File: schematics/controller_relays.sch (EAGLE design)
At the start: 6 parts, among them K1 D1225, K2 D1225, K3 D1225

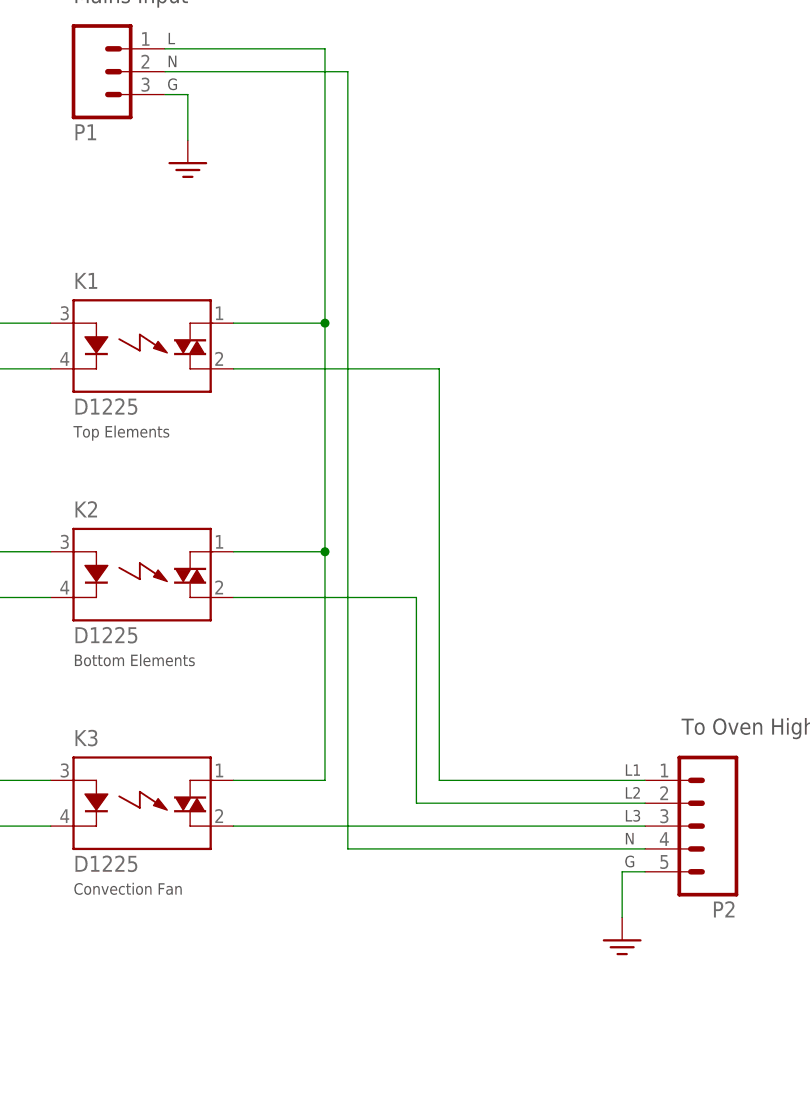
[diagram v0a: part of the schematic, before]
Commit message: Update earth and chassis ground symbols.
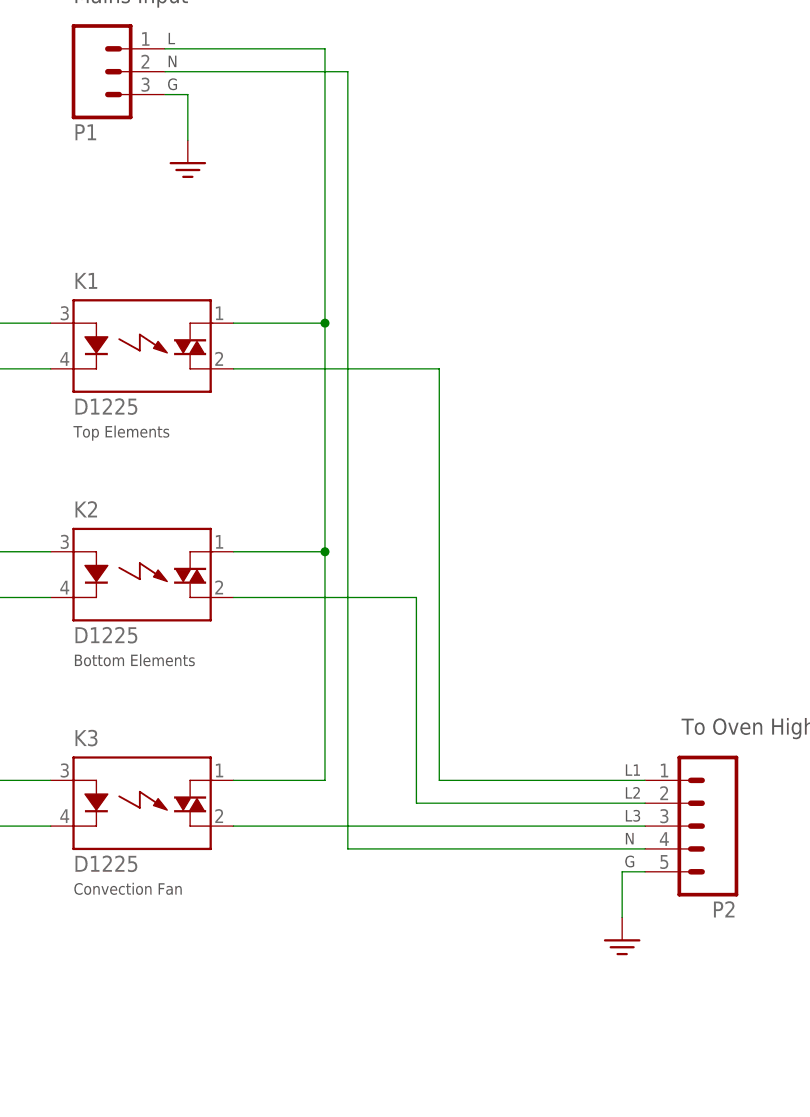
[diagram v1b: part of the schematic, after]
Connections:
- net 3.3V renamed GND
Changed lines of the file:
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@@
 <part name="P1" library="con-amp-quick" library_urn="urn:adsk.eagle:library:125" deviceset="MA03" device="" package3d_urn="urn:adsk.eagle:package:5957/1"/>
 <part name="P2" library="con-amp-quick" library_urn="urn:adsk.eagle:library:125" deviceset="MA05" device="" package3d_urn="urn:adsk.eagle:package:5972/1"/>
-<part name="GND1" library="SparkFun-PowerSymbols" deviceset="GND2" device="" value=""/>
-<part name="GND2" library="SparkFun-PowerSymbols" deviceset="GND2" device="" value=""/>
+<part name="GND1" library="supply" deviceset="EGND" device=""/>
+<part name="GND2" library="supply" deviceset="EGND" device=""/>
 </parts>
 <sheets>
@@
 <instance part="P1" gate="G$1" x="121.92" y="152.4" rot="MR180"/>
 <instance part="P2" gate="G$1" x="190.5" y="68.58" rot="R180"/>
-<instance part="GND1" gate="G$1" x="132.08" y="142.24"/>
-<instance part="GND2" gate="G$1" x="180.34" y="55.88"/>
+<instance part="GND1" gate="1" x="132.08" y="142.24"/>
+<instance part="GND2" gate="1" x="180.34" y="55.88"/>
 </instances>
 <busses>
@@
 <pinref part="K1" gate="G$1" pin="K"/>
 <wire x1="96.52" y1="119.38" x2="116.84" y2="119.38" width="0.1524" layer="91"/>
-</segment>
-</net>
-<net name="3.3V" class="0">
-<segment>
-<pinref part="P1" gate="G$1" pin="3"/>
-<pinref part="GND1" gate="G$1" pin="3.3V"/>
-<wire x1="129.54" y1="149.86" x2="132.08" y2="149.86" width="0.1524" layer="91"/>
-<wire x1="132.08" y1="149.86" x2="132.08" y2="144.78" width="0.1524" layer="91"/>
-</segment>
-<segment>
-<pinref part="P2" gate="G$1" pin="5"/>
-<pinref part="GND2" gate="G$1" pin="3.3V"/>
-<wire x1="182.88" y1="63.5" x2="180.34" y2="63.5" width="0.1524" layer="91"/>
-<wire x1="180.34" y1="63.5" x2="180.34" y2="58.42" width="0.1524" layer="91"/>
 </segment>
 </net>
@@
 </segment>
 </net>
+<net name="GND" class="0">
+<segment>
+<pinref part="P1" gate="G$1" pin="3"/>
+<wire x1="129.54" y1="149.86" x2="132.08" y2="149.86" width="0.1524" layer="91"/>
+<wire x1="132.08" y1="149.86" x2="132.08" y2="144.78" width="0.1524" layer="91"/>
+<pinref part="GND1" gate="1" pin="GND"/>
+</segment>
+<segment>
+<pinref part="P2" gate="G$1" pin="5"/>
+<wire x1="182.88" y1="63.5" x2="180.34" y2="63.5" width="0.1524" layer="91"/>
+<wire x1="180.34" y1="63.5" x2="180.34" y2="58.42" width="0.1524" layer="91"/>
+<pinref part="GND2" gate="1" pin="GND"/>
+</segment>
+</net>
